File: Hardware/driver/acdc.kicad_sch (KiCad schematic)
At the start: 11 parts, among them J401 TBP02R2W-381-03BE, J402 Conn_01x02_Male

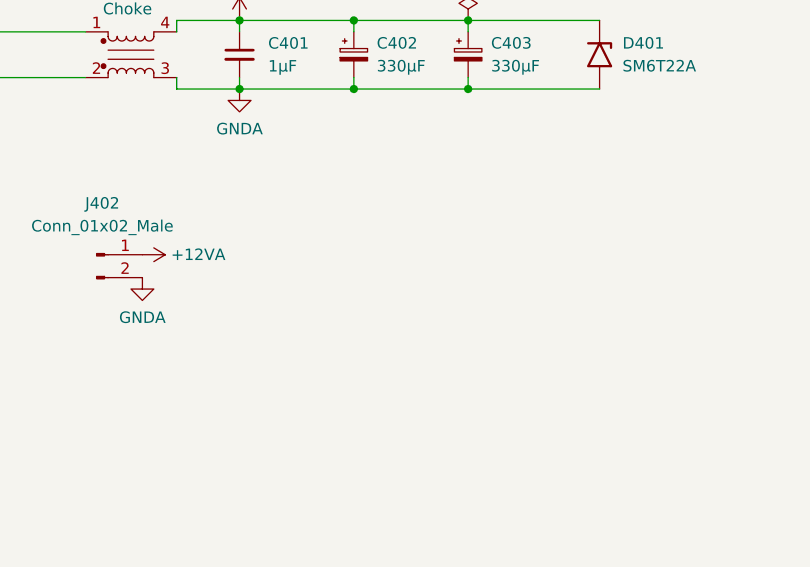
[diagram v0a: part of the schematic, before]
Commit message: Mostly finished routing driver board
- All traces are routed (including some big ass planes for the power
  section; these should be good to roughly 40A) and the board is
  probably good to go.

  It could use with some decorating in the bonus area though :)
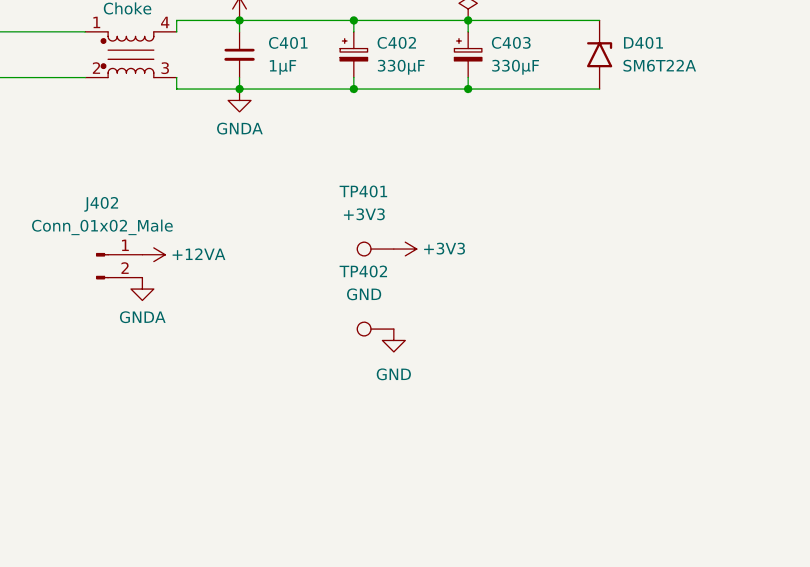
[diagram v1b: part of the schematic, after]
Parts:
- added TP401: +3V3, TestPoint:TestPoint_Keystone_5000-5004_Miniature, symbol Connector:TestPoint
- added TP402: GND, TestPoint:TestPoint_Keystone_5000-5004_Miniature, symbol Connector:TestPoint
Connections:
- new net +3V3: TP401.1
- new net GND: TP402.1
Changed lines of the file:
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@@
     (pin "2")
+  )
+  (symbol (lib_id "Connector:TestPoint") (at 144.78 72.39 90) (mirror x) (unit 1)
+    (in_bom yes) (on_board yes) (fields_autoplaced)
+    (property "Reference" "TP402" (id 0) (at 141.478 66.04 90))
+    (property "Value" "GND" (id 1) (at 141.478 68.58 90))
+    (property "Footprint" "TestPoint:TestPoint_Keystone_5000-5004_Miniature" (id 2) (at 144.78 77.47 0)
+      (effects (font (size 1.27 1.27)) hide)
+    )
+    (property "Datasheet" "~" (id 3) (at 144.78 77.47 0)
+      (effects (font (size 1.27 1.27)) hide)
+    )
+    (property "Color" "Black" (id 4) (at 144.78 72.39 0)
+      (effects (font (size 1.27 1.27)) hide)
+    )
+    (property "MPN" "5001" (id 5) (at 144.78 72.39 0)
+      (effects (font (size 1.27 1.27)) hide)
+    )
+    (pin "1")
   )
   (symbol (lib_id "programmable-load:PSK-S20C-12") (at 85.09 41.91 0) (unit 1)
@@
     (pin "2")
   )
+  (symbol (lib_id "power:+3V3") (at 144.78 63.5 270) (unit 1)
+    (in_bom yes) (on_board yes)
+    (property "Reference" "#PWR0405" (id 0) (at 140.97 63.5 0)
+      (effects (font (size 1.27 1.27)) hide)
+    )
+    (property "Value" "+3V3" (id 1) (at 147.955 63.5 90)
+      (effects (font (size 1.27 1.27)) (justify left))
+    )
+    (property "Footprint" "" (id 2) (at 144.78 63.5 0)
+      (effects (font (size 1.27 1.27)) hide)
+    )
+    (property "Datasheet" "" (id 3) (at 144.78 63.5 0)
+      (effects (font (size 1.27 1.27)) hide)
+    )
+    (pin "1")
+  )
   (symbol (lib_id "Device:C_Polarized_Small") (at 153.035 41.91 0) (unit 1)
     (in_bom yes) (on_board yes)
@@
     )
     (property "Datasheet" "" (id 3) (at 116.84 64.135 0)
+      (effects (font (size 1.27 1.27)) hide)
+    )
+    (pin "1")
+  )
+  (symbol (lib_id "power:GND") (at 144.78 72.39 0) (unit 1)
+    (in_bom yes) (on_board yes) (fields_autoplaced)
+    (property "Reference" "#PWR0406" (id 0) (at 144.78 78.74 0)
+      (effects (font (size 1.27 1.27)) hide)
+    )
+    (property "Value" "GND" (id 1) (at 144.78 77.47 0))
+    (property "Footprint" "" (id 2) (at 144.78 72.39 0)
+      (effects (font (size 1.27 1.27)) hide)
+    )
+    (property "Datasheet" "" (id 3) (at 144.78 72.39 0)
       (effects (font (size 1.27 1.27)) hide)
     )
@@
     (pin "2")
   )
+  (symbol (lib_id "Connector:TestPoint") (at 144.78 63.5 90) (mirror x) (unit 1)
+    (in_bom yes) (on_board yes) (fields_autoplaced)
+    (property "Reference" "TP401" (id 0) (at 141.478 57.15 90))
+    (property "Value" "+3V3" (id 1) (at 141.478 59.69 90))
+    (property "Footprint" "TestPoint:TestPoint_Keystone_5000-5004_Miniature" (id 2) (at 144.78 68.58 0)
+      (effects (font (size 1.27 1.27)) hide)
+    )
+    (property "Datasheet" "~" (id 3) (at 144.78 68.58 0)
+      (effects (font (size 1.27 1.27)) hide)
+    )
+    (property "Color" "Red" (id 4) (at 144.78 63.5 0)
+      (effects (font (size 1.27 1.27)) hide)
+    )
+    (property "MPN" "5000" (id 5) (at 144.78 63.5 0)
+      (effects (font (size 1.27 1.27)) hide)
+    )
+    (pin "1")
+  )
   (symbol (lib_id "power:GNDA") (at 116.84 66.675 0) (unit 1)

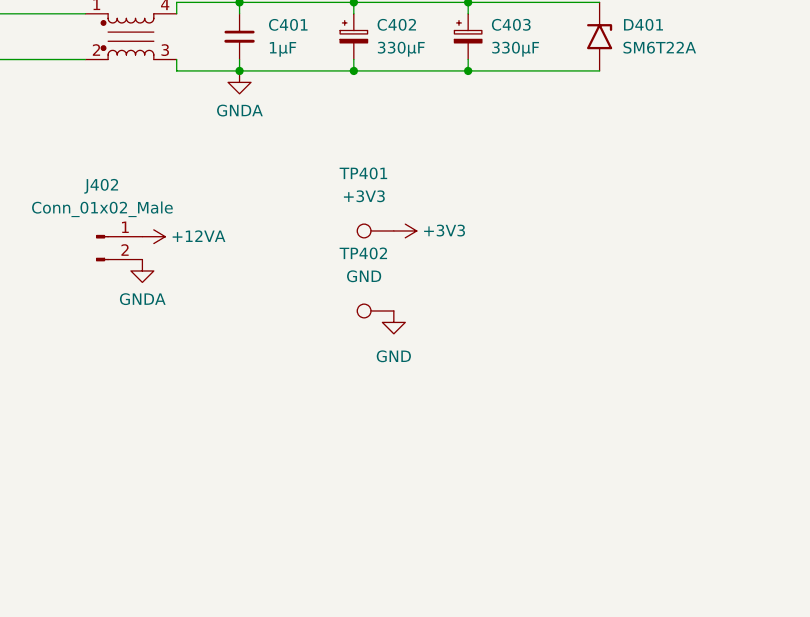
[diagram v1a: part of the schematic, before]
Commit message: Minor tweaks to layout/schematic
- Use a DC/DC to generate 5V, then generate 3V3 via an LDO from that:
  this should help filter out more of the switching noise out of the
  supplies.

  Also, this included adding a 330Ω load resistor so that the DC/DC gets
  the minimum load it expects; it burns ~15mA at 5V.

- Changes to pass DRC
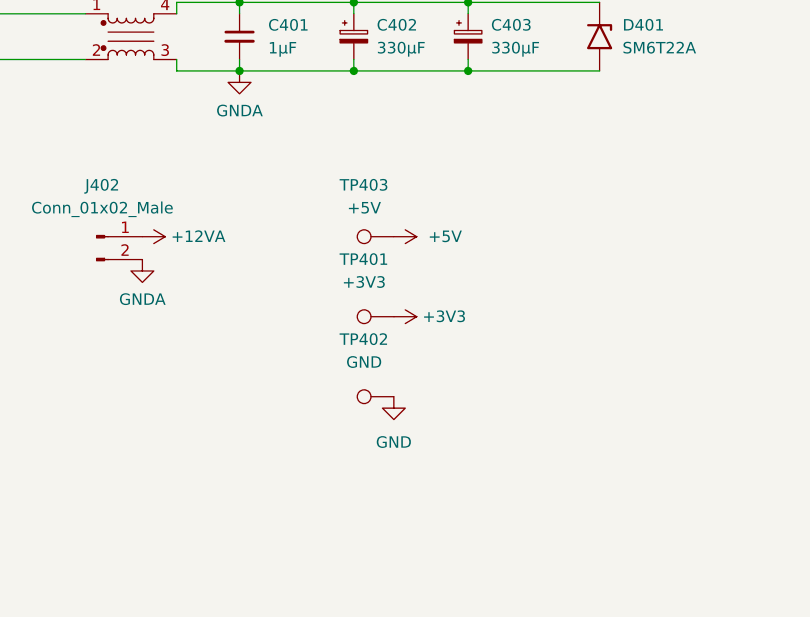
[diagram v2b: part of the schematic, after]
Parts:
- added TP403: +5V, TestPoint:TestPoint_Keystone_5000-5004_Miniature, symbol Connector:TestPoint
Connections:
- new net +5V: TP403.1
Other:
- moved on the sheet: TP401, TP402
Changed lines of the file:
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@@
     (pin "2")
   )
-  (symbol (lib_id "Connector:TestPoint") (at 144.78 72.39 90) (mirror x) (unit 1)
-    (in_bom yes) (on_board yes) (fields_autoplaced)
-    (property "Reference" "TP402" (id 0) (at 141.478 66.04 90))
-    (property "Value" "GND" (id 1) (at 141.478 68.58 90))
-    (property "Footprint" "TestPoint:TestPoint_Keystone_5000-5004_Miniature" (id 2) (at 144.78 77.47 0)
-      (effects (font (size 1.27 1.27)) hide)
-    )
-    (property "Datasheet" "~" (id 3) (at 144.78 77.47 0)
-      (effects (font (size 1.27 1.27)) hide)
-    )
-    (property "Color" "Black" (id 4) (at 144.78 72.39 0)
-      (effects (font (size 1.27 1.27)) hide)
-    )
-    (property "MPN" "5001" (id 5) (at 144.78 72.39 0)
+  (symbol (lib_id "Connector:TestPoint") (at 144.78 81.915 90) (mirror x) (unit 1)
+    (in_bom yes) (on_board yes) (fields_autoplaced)
+    (property "Reference" "TP402" (id 0) (at 141.478 75.565 90))
+    (property "Value" "GND" (id 1) (at 141.478 78.105 90))
+    (property "Footprint" "TestPoint:TestPoint_Keystone_5000-5004_Miniature" (id 2) (at 144.78 86.995 0)
+      (effects (font (size 1.27 1.27)) hide)
+    )
+    (property "Datasheet" "~" (id 3) (at 144.78 86.995 0)
+      (effects (font (size 1.27 1.27)) hide)
+    )
+    (property "Color" "Black" (id 4) (at 144.78 81.915 0)
+      (effects (font (size 1.27 1.27)) hide)
+    )
+    (property "MPN" "5001" (id 5) (at 144.78 81.915 0)
       (effects (font (size 1.27 1.27)) hide)
     )
@@
     (pin "2")
   )
-  (symbol (lib_id "power:+3V3") (at 144.78 63.5 270) (unit 1)
-    (in_bom yes) (on_board yes)
-    (property "Reference" "#PWR0405" (id 0) (at 140.97 63.5 0)
-      (effects (font (size 1.27 1.27)) hide)
-    )
-    (property "Value" "+3V3" (id 1) (at 147.955 63.5 90)
-      (effects (font (size 1.27 1.27)) (justify left))
-    )
-    (property "Footprint" "" (id 2) (at 144.78 63.5 0)
-      (effects (font (size 1.27 1.27)) hide)
-    )
-    (property "Datasheet" "" (id 3) (at 144.78 63.5 0)
+  (symbol (lib_id "power:+3V3") (at 144.78 73.025 270) (unit 1)
+    (in_bom yes) (on_board yes)
+    (property "Reference" "#PWR0405" (id 0) (at 140.97 73.025 0)
+      (effects (font (size 1.27 1.27)) hide)
+    )
+    (property "Value" "+3V3" (id 1) (at 147.955 73.025 90)
+      (effects (font (size 1.27 1.27)) (justify left))
+    )
+    (property "Footprint" "" (id 2) (at 144.78 73.025 0)
+      (effects (font (size 1.27 1.27)) hide)
+    )
+    (property "Datasheet" "" (id 3) (at 144.78 73.025 0)
       (effects (font (size 1.27 1.27)) hide)
     )
@@
     (pin "1")
   )
-  (symbol (lib_id "power:GND") (at 144.78 72.39 0) (unit 1)
-    (in_bom yes) (on_board yes) (fields_autoplaced)
-    (property "Reference" "#PWR0406" (id 0) (at 144.78 78.74 0)
-      (effects (font (size 1.27 1.27)) hide)
-    )
-    (property "Value" "GND" (id 1) (at 144.78 77.47 0))
-    (property "Footprint" "" (id 2) (at 144.78 72.39 0)
-      (effects (font (size 1.27 1.27)) hide)
-    )
-    (property "Datasheet" "" (id 3) (at 144.78 72.39 0)
+  (symbol (lib_id "power:GND") (at 144.78 81.915 0) (unit 1)
+    (in_bom yes) (on_board yes) (fields_autoplaced)
+    (property "Reference" "#PWR0406" (id 0) (at 144.78 88.265 0)
+      (effects (font (size 1.27 1.27)) hide)
+    )
+    (property "Value" "GND" (id 1) (at 144.78 86.995 0))
+    (property "Footprint" "" (id 2) (at 144.78 81.915 0)
+      (effects (font (size 1.27 1.27)) hide)
+    )
+    (property "Datasheet" "" (id 3) (at 144.78 81.915 0)
       (effects (font (size 1.27 1.27)) hide)
     )
@@
     )
     (property "Datasheet" "" (id 3) (at 127.635 45.72 0)
+      (effects (font (size 1.27 1.27)) hide)
+    )
+    (pin "1")
+  )
+  (symbol (lib_id "power:+5V") (at 144.78 64.135 270) (unit 1)
+    (in_bom yes) (on_board yes) (fields_autoplaced)
+    (property "Reference" "#PWR0407" (id 0) (at 140.97 64.135 0)
+      (effects (font (size 1.27 1.27)) hide)
+    )
+    (property "Value" "+5V" (id 1) (at 148.59 64.1349 90)
+      (effects (font (size 1.27 1.27)) (justify left))
+    )
+    (property "Footprint" "" (id 2) (at 144.78 64.135 0)
+      (effects (font (size 1.27 1.27)) hide)
+    )
+    (property "Datasheet" "" (id 3) (at 144.78 64.135 0)
       (effects (font (size 1.27 1.27)) hide)
     )
@@
     (pin "2")
   )
-  (symbol (lib_id "Connector:TestPoint") (at 144.78 63.5 90) (mirror x) (unit 1)
-    (in_bom yes) (on_board yes) (fields_autoplaced)
-    (property "Reference" "TP401" (id 0) (at 141.478 57.15 90))
-    (property "Value" "+3V3" (id 1) (at 141.478 59.69 90))
-    (property "Footprint" "TestPoint:TestPoint_Keystone_5000-5004_Miniature" (id 2) (at 144.78 68.58 0)
-      (effects (font (size 1.27 1.27)) hide)
-    )
-    (property "Datasheet" "~" (id 3) (at 144.78 68.58 0)
-      (effects (font (size 1.27 1.27)) hide)
-    )
-    (property "Color" "Red" (id 4) (at 144.78 63.5 0)
-      (effects (font (size 1.27 1.27)) hide)
-    )
-    (property "MPN" "5000" (id 5) (at 144.78 63.5 0)
+  (symbol (lib_id "Connector:TestPoint") (at 144.78 73.025 90) (mirror x) (unit 1)
+    (in_bom yes) (on_board yes) (fields_autoplaced)
+    (property "Reference" "TP401" (id 0) (at 141.478 66.675 90))
+    (property "Value" "+3V3" (id 1) (at 141.478 69.215 90))
+    (property "Footprint" "TestPoint:TestPoint_Keystone_5000-5004_Miniature" (id 2) (at 144.78 78.105 0)
+      (effects (font (size 1.27 1.27)) hide)
+    )
+    (property "Datasheet" "~" (id 3) (at 144.78 78.105 0)
+      (effects (font (size 1.27 1.27)) hide)
+    )
+    (property "Color" "Red" (id 4) (at 144.78 73.025 0)
+      (effects (font (size 1.27 1.27)) hide)
+    )
+    (property "MPN" "5000" (id 5) (at 144.78 73.025 0)
       (effects (font (size 1.27 1.27)) hide)
     )
@@
     (pin "2")
   )
+  (symbol (lib_id "Connector:TestPoint") (at 144.78 64.135 90) (mirror x) (unit 1)
+    (in_bom yes) (on_board yes) (fields_autoplaced)
+    (property "Reference" "TP403" (id 0) (at 141.478 58.42 90))
+    (property "Value" "+5V" (id 1) (at 141.478 60.96 90))
+    (property "Footprint" "TestPoint:TestPoint_Keystone_5000-5004_Miniature" (id 2) (at 144.78 69.215 0)
+      (effects (font (size 1.27 1.27)) hide)
+    )
+    (property "Datasheet" "~" (id 3) (at 144.78 69.215 0)
+      (effects (font (size 1.27 1.27)) hide)
+    )
+    (property "Color" "Red" (id 4) (at 144.78 64.135 0)
+      (effects (font (size 1.27 1.27)) hide)
+    )
+    (property "MPN" "5000" (id 5) (at 144.78 64.135 0)
+      (effects (font (size 1.27 1.27)) hide)
+    )
+    (pin "1")
+  )
 )

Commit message: Driver current zero adjustment
- Added facility on the driver board to adjust the zero offset for the
  current drive op amps, to allow them to actually reach zero when a
  zero DAC code is input to them.

  This is done by means of a -5V supply (generated with switched
  capacitor regulator) and each output amplifier having a -2.5V
  reference, and an associated multi-turn trim pot to actually trim
  that; these are hooked up to 3V3 digital on the other end (this should
  probably be the DAC reference but we don't have ez access to that)
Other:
- title: (none) -> Dual Programmable Load Driver
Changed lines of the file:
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@@
   (paper "A4")
   (title_block
+    (title "Dual Programmable Load Driver")
+    (date "2022-03-10")
+    (rev "1")
     (comment 1 "AC/DC mains supply to generate 12V")
     (comment 2 "Omit all components (except D402, R401) if not using built in mains switching supply")
